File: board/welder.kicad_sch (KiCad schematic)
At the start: 47 parts, among them J1 48 VDC INPUT, Q1 Q_NIGBT_GCE, Q2 Q_NIGBT_GCE, Q3 Q_NIGBT_GCE, Q4 Q_NIGBT_GCE, U2 mEZD71201A-F, U3 MIC4604YM, U4 MIC4604YM

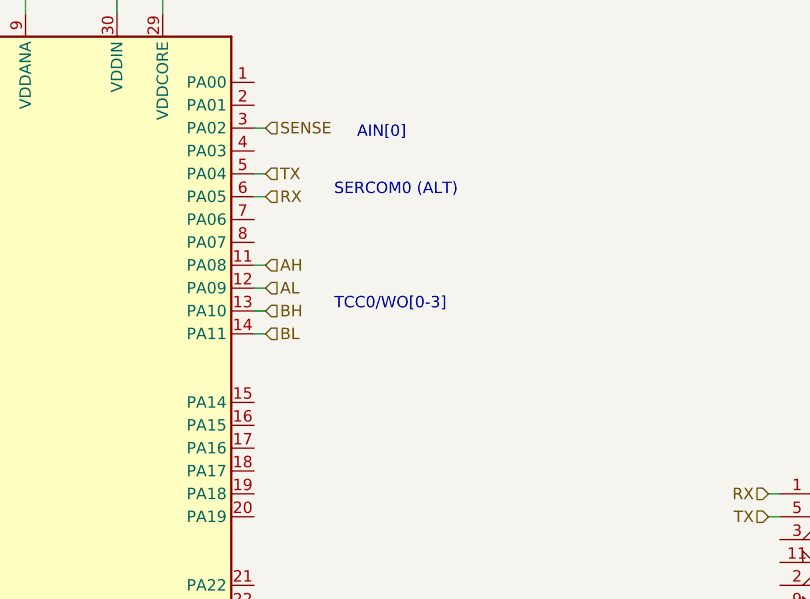
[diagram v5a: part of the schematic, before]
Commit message: Moved *H and *L signals to complementary outputs for DTI
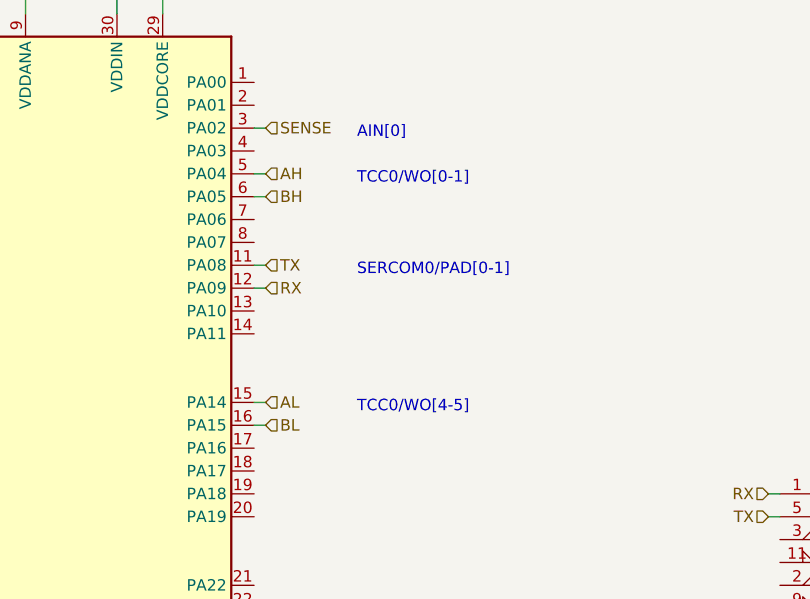
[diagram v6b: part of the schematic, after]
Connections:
- net AH: now also U?.5 (PA04); no longer U?.11 (PA08)
- net AL: now also U?.15 (PA14); no longer U?.12 (PA09)
- net BH: now also U?.6 (PA05); no longer U?.13 (PA10)
- net BL: now also U?.16 (PA15); no longer U?.14 (PA11)
- net RX: now also U?.12 (PA09); no longer U?.6 (PA05)
- net TX: now also U?.11 (PA08); no longer U?.5 (PA04)
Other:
- note added: "SERCOM0/PAD[0-1]"
- note added: "TCC0/WO[0-1]"
- note added: "TCC0/WO[4-5]"
- note removed: "SERCOM0 (ALT)"
- note removed: "TCC0/WO[0-3]"
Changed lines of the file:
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@@
     (stroke (width 0) (type default) (color 0 0 0 0))
   )
-  (wire (pts (xy 73.66 187.96) (xy 72.39 187.96))
+  (wire (pts (xy 73.66 175.26) (xy 72.39 175.26))
     (stroke (width 0) (type default) (color 0 0 0 0))
   )
@@
     (stroke (width 0) (type default) (color 0 0 0 0))
   )
-  (wire (pts (xy 73.66 175.26) (xy 72.39 175.26))
+  (wire (pts (xy 73.66 185.42) (xy 72.39 185.42))
     (stroke (width 0) (type default) (color 0 0 0 0))
   )
@@
     (stroke (width 0) (type default) (color 0 0 0 0))
   )
-  (wire (pts (xy 73.66 185.42) (xy 72.39 185.42))
+  (wire (pts (xy 73.66 198.12) (xy 72.39 198.12))
     (stroke (width 0) (type default) (color 0 0 0 0))
   )
@@
     (stroke (width 0) (type default) (color 0 0 0 0))
   )
+  (wire (pts (xy 73.66 172.72) (xy 72.39 172.72))
+    (stroke (width 0) (type default) (color 0 0 0 0))
+  )
+  (wire (pts (xy 66.04 125.73) (xy 67.31 125.73))
+    (stroke (width 0) (type default) (color 0 0 0 0))
+  )
+  (wire (pts (xy 38.1 138.43) (xy 36.83 138.43))
+    (stroke (width 0) (type default) (color 0 0 0 0))
+  )
+  (wire (pts (xy 59.69 102.87) (xy 58.42 102.87))
+    (stroke (width 0) (type default) (color 0 0 0 0))
+  )
+  (wire (pts (xy 73.66 200.66) (xy 72.39 200.66))
+    (stroke (width 0) (type default) (color 0 0 0 0))
+  )
+  (wire (pts (xy 346.71 87.63) (xy 346.71 86.36))
+    (stroke (width 0) (type default) (color 0 0 0 0))
+  )
+  (wire (pts (xy 325.12 101.6) (xy 326.39 101.6))
+    (stroke (width 0) (type default) (color 0 0 0 0))
+  )
+  (wire (pts (xy 162.56 191.77) (xy 162.56 193.04))
+    (stroke (width 0) (type default) (color 0 0 0 0))
+  )
+  (wire (pts (xy 325.12 40.64) (xy 330.2 40.64))
+    (stroke (width 0) (type default) (color 0 0 0 0))
+  )
+  (wire (pts (xy 330.2 55.88) (xy 341.63 55.88))
+    (stroke (width 0) (type default) (color 0 0 0 0))
+  )
+  (wire (pts (xy 378.46 100.33) (xy 377.19 100.33))
+    (stroke (width 0) (type default) (color 0 0 0 0))
+  )
+  (wire (pts (xy 231.14 226.06) (xy 231.14 227.33))
+    (stroke (width 0) (type default) (color 0 0 0 0))
+  )
+  (wire (pts (xy 151.13 38.1) (xy 151.13 39.37))
+    (stroke (width 0) (type default) (color 0 0 0 0))
+  )
+  (wire (pts (xy 341.63 160.02) (xy 341.63 161.29))
+    (stroke (width 0) (type default) (color 0 0 0 0))
+  )
+  (wire (pts (xy 378.46 100.33) (xy 379.73 100.33))
+    (stroke (width 0) (type default) (color 0 0 0 0))
+  )
+  (wire (pts (xy 151.13 252.73) (xy 151.13 251.46))
+    (stroke (width 0) (type default) (color 0 0 0 0))
+  )
+  (wire (pts (xy 38.1 151.13) (xy 36.83 151.13))
+    (stroke (width 0) (type default) (color 0 0 0 0))
+  )
   (wire (pts (xy 73.66 182.88) (xy 72.39 182.88))
     (stroke (width 0) (type default) (color 0 0 0 0))
   )
-  (wire (pts (xy 66.04 125.73) (xy 67.31 125.73))
-    (stroke (width 0) (type default) (color 0 0 0 0))
-  )
-  (wire (pts (xy 38.1 138.43) (xy 36.83 138.43))
-    (stroke (width 0) (type default) (color 0 0 0 0))
-  )
-  (wire (pts (xy 59.69 102.87) (xy 58.42 102.87))
-    (stroke (width 0) (type default) (color 0 0 0 0))
-  )
-  (wire (pts (xy 73.66 190.5) (xy 72.39 190.5))
-    (stroke (width 0) (type default) (color 0 0 0 0))
-  )
-  (wire (pts (xy 346.71 87.63) (xy 346.71 86.36))
-    (stroke (width 0) (type default) (color 0 0 0 0))
-  )
-  (wire (pts (xy 325.12 101.6) (xy 326.39 101.6))
-    (stroke (width 0) (type default) (color 0 0 0 0))
-  )
-  (wire (pts (xy 162.56 191.77) (xy 162.56 193.04))
-    (stroke (width 0) (type default) (color 0 0 0 0))
-  )
-  (wire (pts (xy 325.12 40.64) (xy 330.2 40.64))
-    (stroke (width 0) (type default) (color 0 0 0 0))
-  )
-  (wire (pts (xy 330.2 55.88) (xy 341.63 55.88))
-    (stroke (width 0) (type default) (color 0 0 0 0))
-  )
-  (wire (pts (xy 378.46 100.33) (xy 377.19 100.33))
-    (stroke (width 0) (type default) (color 0 0 0 0))
-  )
-  (wire (pts (xy 231.14 226.06) (xy 231.14 227.33))
-    (stroke (width 0) (type default) (color 0 0 0 0))
-  )
-  (wire (pts (xy 151.13 38.1) (xy 151.13 39.37))
-    (stroke (width 0) (type default) (color 0 0 0 0))
-  )
-  (wire (pts (xy 341.63 160.02) (xy 341.63 161.29))
-    (stroke (width 0) (type default) (color 0 0 0 0))
-  )
-  (wire (pts (xy 378.46 100.33) (xy 379.73 100.33))
-    (stroke (width 0) (type default) (color 0 0 0 0))
-  )
-  (wire (pts (xy 151.13 252.73) (xy 151.13 251.46))
-    (stroke (width 0) (type default) (color 0 0 0 0))
-  )
-  (wire (pts (xy 38.1 151.13) (xy 36.83 151.13))
-    (stroke (width 0) (type default) (color 0 0 0 0))
-  )
-  (wire (pts (xy 73.66 172.72) (xy 72.39 172.72))
-    (stroke (width 0) (type default) (color 0 0 0 0))
-  )
   (wire (pts (xy 346.71 64.77) (xy 354.33 64.77))
     (stroke (width 0) (type default) (color 0 0 0 0))
@@
     (stroke (width 0) (type default) (color 0 0 0 0))
   )
-  (text "TCC0/WO[0-3]" (at 81.28 187.96 0)
+  (text "TCC0/WO[4-5]" (at 83.82 199.39 0)
     (effects (font (size 1.27 1.27)) (justify left bottom))
   )
-  (text "SERCOM0 (ALT)" (at 81.28 175.26 0)
+  (text "TCC0/WO[0-1]" (at 83.82 173.99 0)
+    (effects (font (size 1.27 1.27)) (justify left bottom))
+  )
+  (text "SERCOM0/PAD[0-1]" (at 83.82 184.15 0)
     (effects (font (size 1.27 1.27)) (justify left bottom))
   )
@@
     (effects (font (size 1.27 1.27)) (justify left bottom))
   )
-  (hierarchical_label "TX" (shape input) (at 73.66 172.72 0)
+  (hierarchical_label "TX" (shape input) (at 73.66 182.88 0)
     (effects (font (size 1.27 1.27)) (justify left))
   )
@@
     (effects (font (size 1.27 1.27)) (justify right))
   )
-  (hierarchical_label "AH" (shape input) (at 73.66 182.88 0)
+  (hierarchical_label "AH" (shape input) (at 73.66 172.72 0)
     (effects (font (size 1.27 1.27)) (justify left))
   )
@@
     (effects (font (size 1.27 1.27)) (justify left))
   )
-  (hierarchical_label "BH" (shape input) (at 73.66 187.96 0)
+  (hierarchical_label "BH" (shape input) (at 73.66 175.26 0)
     (effects (font (size 1.27 1.27)) (justify left))
   )
@@
     (effects (font (size 1.27 1.27)) (justify right))
   )
-  (hierarchical_label "BL" (shape input) (at 73.66 190.5 0)
+  (hierarchical_label "BL" (shape input) (at 73.66 200.66 0)
     (effects (font (size 1.27 1.27)) (justify left))
   )
@@
     (effects (font (size 1.27 1.27)) (justify right))
   )
-  (hierarchical_label "RX" (shape input) (at 73.66 175.26 0)
+  (hierarchical_label "RX" (shape input) (at 73.66 185.42 0)
     (effects (font (size 1.27 1.27)) (justify left))
   )
@@
     (effects (font (size 1.27 1.27)) (justify left))
   )
-  (hierarchical_label "AL" (shape input) (at 73.66 185.42 0)
-    (effects (font (size 1.27 1.27)) (justify left))
-  )
+  (hierarchical_label "AL" (shape input) (at 73.66 198.12 0)
+    (effects (font (size 1.27 1.27)) (justify left))
+  )

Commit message: Annotated schematic
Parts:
- gave numbers to parts that had none: 29

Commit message: Updated PNs and footprints
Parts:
- removed J1: 48 VDC INPUT, symbol Connector_Generic:Conn_01x02
- added J1: VIN, MountingHole:MountingHole_6.4mm_M6_Pad, symbol Connector_Generic:Conn_01x01
- added J7: GND, MountingHole:MountingHole_6.4mm_M6_Pad, symbol Connector_Generic:Conn_01x01
- C1, C2, C3, C4: footprint (none) -> Capacitor_SMD:C_1210_3225Metric; description (none) -> MLCC, 4.7 uF, 100 V, X7R, 1210
- C10, C7: footprint Capacitor_SMD:C_0603_1608Metric -> Capacitor_SMD:C_0805_2012Metric; MFG1 (none) -> KEMET; MFG1PN (none) -> C0805C104M5RACTU; description MLCC, 0.1 uF, 16 V, X7R, 0603 -> MLCC, 0.1 uF, 50 V, X7R, 0805; mfg1 KEMET -> (none); mfg1pn C0603C104M4RAC7411 -> (none)
- C11: MFG1 (none) -> Samsung Electro-Mechanics; MFG1PN (none) -> CL21B105KBFNFNE; description MLCC, 1 uF, 16 V, X7R, 0603 -> MLCC, 1 uF, 50 V, X7R, 0805; mfg1 TDK -> (none); mfg1pn CGA3E1X7R1C105K080AC -> (none)
- C12, C13, C6, C8: footprint (none) -> Capacitor_SMD:C_0805_2012Metric; MFG1 (none) -> KEMET; MFG1PN (none) -> C0805C104M5RACTU; description (none) -> MLCC, 0.1 uF, 50 V, X7R, 0805
- C14, C15, C19: value 0.1uF -> 0.1 uF; footprint Capacitor_SMD:C_0603_1608Metric -> Capacitor_SMD:C_0805_2012Metric; MFG1 (none) -> KEMET; MFG1PN (none) -> C0805C104M5RACTU; description (none) -> MLCC, 0.1 uF, 50 V, X7R, 0805
- C16: footprint Capacitor_SMD:C_0603_1608Metric -> Capacitor_SMD:C_0805_2012Metric; MFG1 (none) -> KEMET; MFG1PN (none) -> C0805C104M5RACTU; description (none) -> MLCC, 0.1 uF, 50 V, X7R, 0805
- C17, C18: MFG1 (none) -> KEMET; MFG1PN (none) -> C0805C470J5GAC; description (none) -> MLCC, 47 pF, 50 V, C0G, 0805
- C20: value 47 uF -> 50 uF; MFG1 (none) -> Cornell Dubilier - CDE; MFG1PN (none) -> BLH506K451B104; Voltage 100 V -> 450 V; description (none) -> Film Capacitor, 50 uF, 450 VDC, 230 VAC
- C5, C9: MFG1 (none) -> Samsung Electro-Mechanics; MFG1PN (none) -> CL32B106KBJNNNF; description MLCC, 10 uF, 16 V, X5R, 0603 -> MLCC, 10 uF, 50 V, X7R, 1210; mfg1 Taiyo Yuden -> (none); mfg1pn EMK107BBJ106MA-T -> (none)
- D1, D2, D3, D4: MFG1 (none) -> Rectron; MFG1PN (none) -> 10A10-T; description (none) -> Silicon rectifier diode, 10 A, 1000 V; mfg1 Rectron -> (none); mfg1pn 10A10-T -> (none)
- D5: description (none) -> Schottky diode, 3 A, 450 mV forward
- FB1: MFG1 (none) -> Bourns; MFG1PN (none) -> MU2029-471Y; description Ferrite Bead, 150 Ohm, 750 mA, 0603 -> Ferrite Bead,470 Ohm, 700 mA, 0805; mfg1 Murata Electronics -> (none); mfg1pn BLM18AG151SN1D -> (none)
- J2: MFG1 (none) -> Samtec; MFG1PN (none) -> FTSH-105-01-F-D-RA-K; mfg1 Samtec -> (none); mfg1pn FTSH-105-01-F-D-RA-K -> (none)
- J4: footprint HotMeltTechnologies:USB_B_AMPHENOL_P-UE27-BCX4-XXX_Horizontal -> Connector_USB:USB_B_OST_USB-B1HSxx_Horizontal; MFG1 (none) -> On Shore Technology Inc.; MFG1PN (none) -> USB-B1HSB6
- J5, J6: footprint (none) -> MountingHole:MountingHole_6.4mm_M6_Pad
- Q1, Q2, Q3, Q4: footprint (none) -> Package_TO_SOT_THT:TO-247-3_Vertical
- R1, R2: MFG1 (none) -> Panasonic; MFG1PN (none) -> ERJ-3EKF1003V; mfg1 Panasonic -> (none); mfg1pn ERJ-3EKF1003V -> (none)
- R3: value 100 u -> 0.0001
- U1: MFG1 (none) -> Microchip; MFG1PN (none) -> ATSAMD21E18A-AU
- U2: value mEZD71201A-F -> LD1117ADT33TR; footprint Converter_DCDC:Converter_DCDC_RECOM_R-78E-0.5_THT -> Package_TO_SOT_SMD:TO-252-3_TabPin2; MFG1 Monolithic Power Systems -> STMicroelectronics; MFG1PN mEZD71201A-F -> LD1117ADT33TR
- U3, U4: MFG1 (none) -> Microchip; MFG1PN (none) -> MIC4604YM
- U5: MFG1 (none) -> Recom; MFG1PN (none) -> R-78E5.0-0.5
- U6: MFG1 (none) -> FTDI; MFG1PN (none) -> FT232RL
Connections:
- net +48V: now also J1.1 (Pin_1)
- net GND: now also J7.1 (Pin_1)
